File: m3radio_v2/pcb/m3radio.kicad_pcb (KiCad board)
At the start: 2 copper layers, 40 x 40 mm, 65 parts, among them IC1 NCP380, IC101 STM32F405RxTx, IC102 MCP2562, IC2 NC7SZ04, IC201 Si4460, IC3 CS2100-CP, IC4 SL18860DC, IC5 MAX_M8Q, IC6 SN74LVC1G0832, J101 WEST TOP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

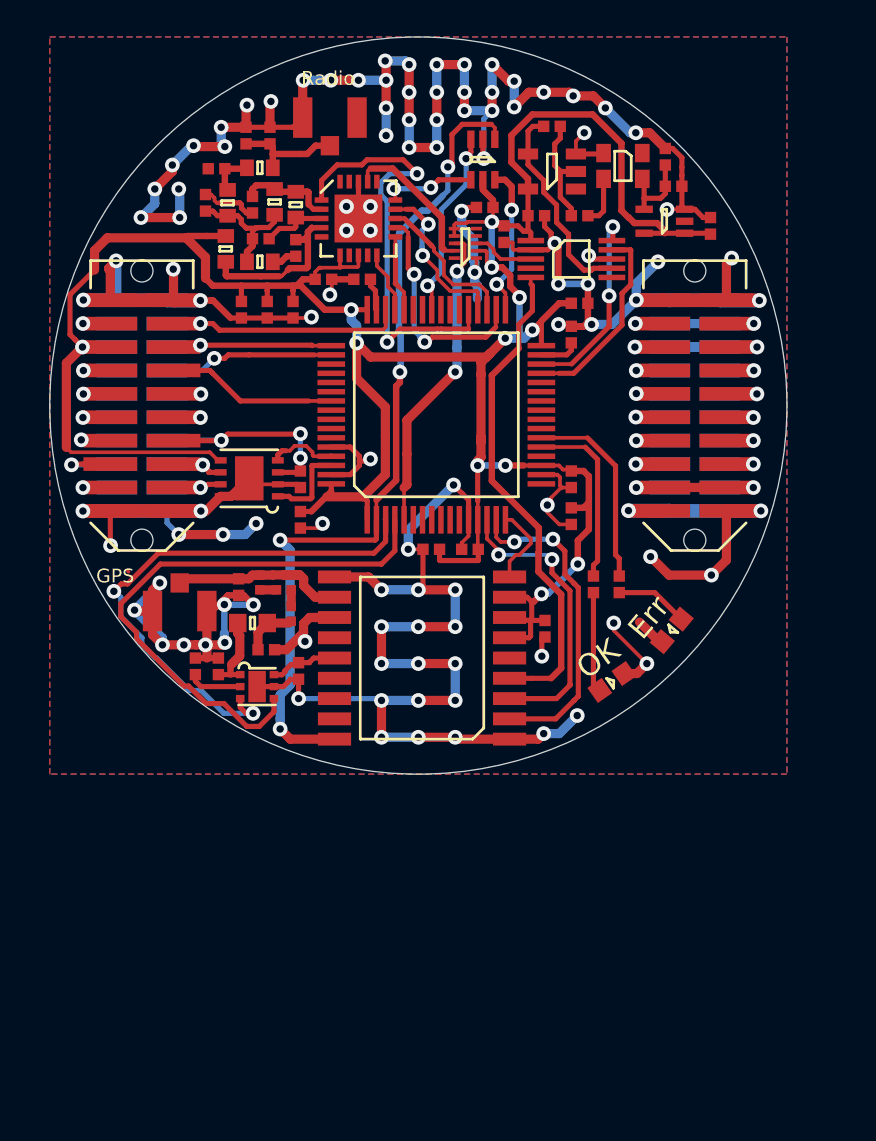
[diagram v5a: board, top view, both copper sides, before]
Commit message: Actually connect gps pps to tim2
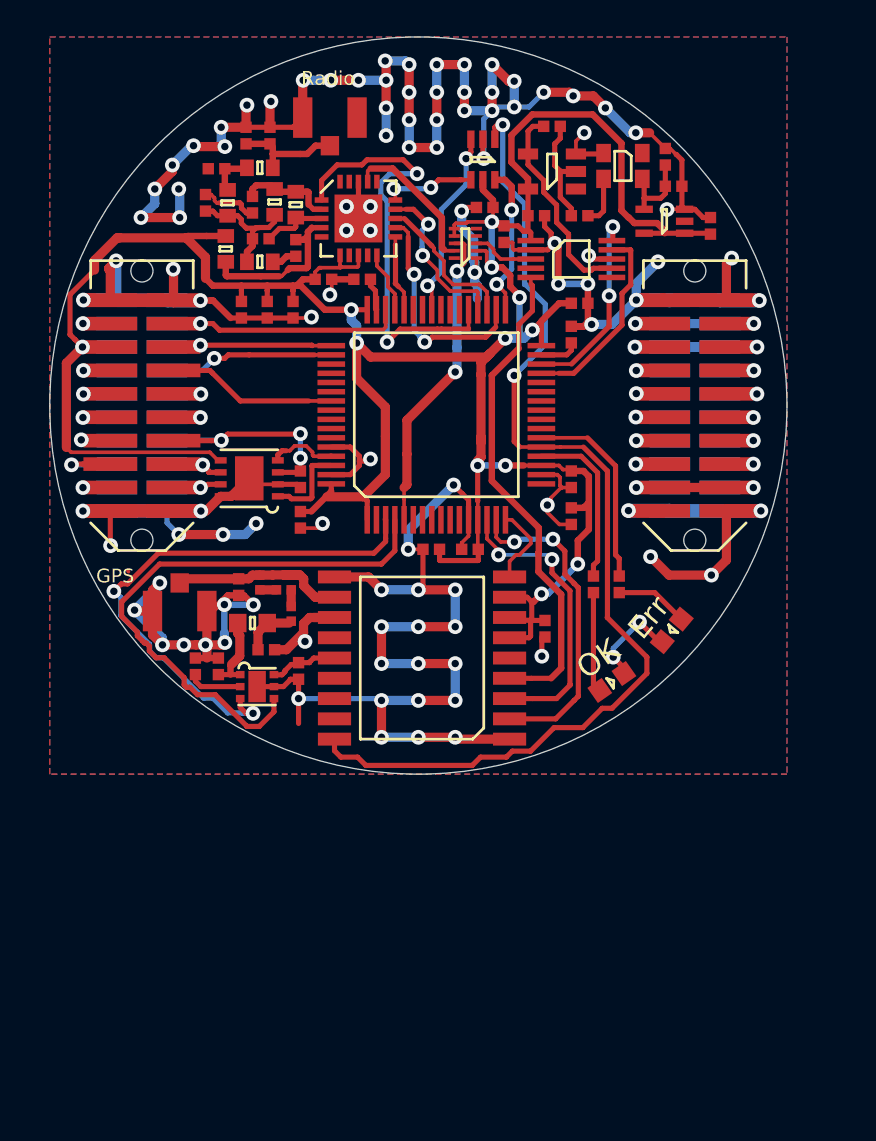
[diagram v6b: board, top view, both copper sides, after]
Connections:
- net /Radio/Radio_GPIO1 renamed /Radio_GPIO1
- net /Radio/Radio_SCLK renamed /Radio_SCLK
- net /Radio/Radio_SDI renamed /Radio_SDI
- net /Radio/Radio_SDN renamed /Radio_SDN
- net /Radio/Radio_SDO renamed /Radio_SDO
- net /Radio/Radio_XIN renamed /Radio_CLK
- net /Radio/Radio_nIRQ renamed /Radio_nIRQ
- IC101 pad 2: /GPS_PPS -> (no net)
- IC101 pad 20: (no net) -> /LED_GRN
- IC101 pad 21: /LED_GRN -> /GPS_PPS
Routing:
- net /GPS_PPS: track 46.3 -> 57.6 mm, vias 4 -> 2
- net GND: track 331.6 -> 328.4 mm, vias 107 -> 104
- net /LED_GRN: track 9.75 -> 9.12 mm

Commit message: Reduce radio board diameter
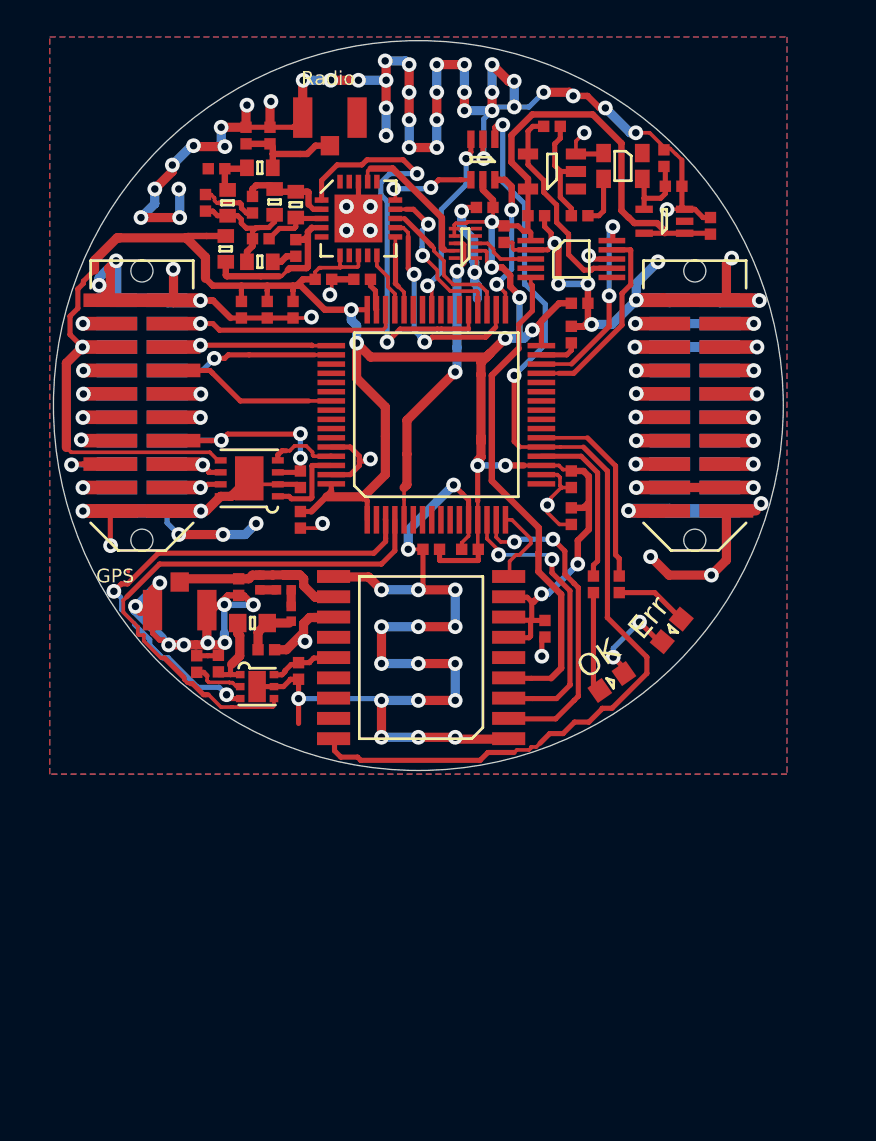
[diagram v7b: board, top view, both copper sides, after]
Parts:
- moved C3 0.15 mm to (89.2, 114.0)
- moved R2 0.15 mm to (88.0, 114.0)
- moved C8 0.11 mm to (113.3, 86.6)
- moved IC5 0.06 mm to (100.2, 113.7)
- moved P101 0.05 mm to (87.0, 111.1)
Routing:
- net GND: track 328.4 -> 331.2 mm
- net /ANT_~FLAG: track 29.5 -> 26.9 mm
- net /ANT_~EN: track 30.7 -> 29.4 mm
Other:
- board size 40 x 40 mm -> 39.6 x 39.6 mm

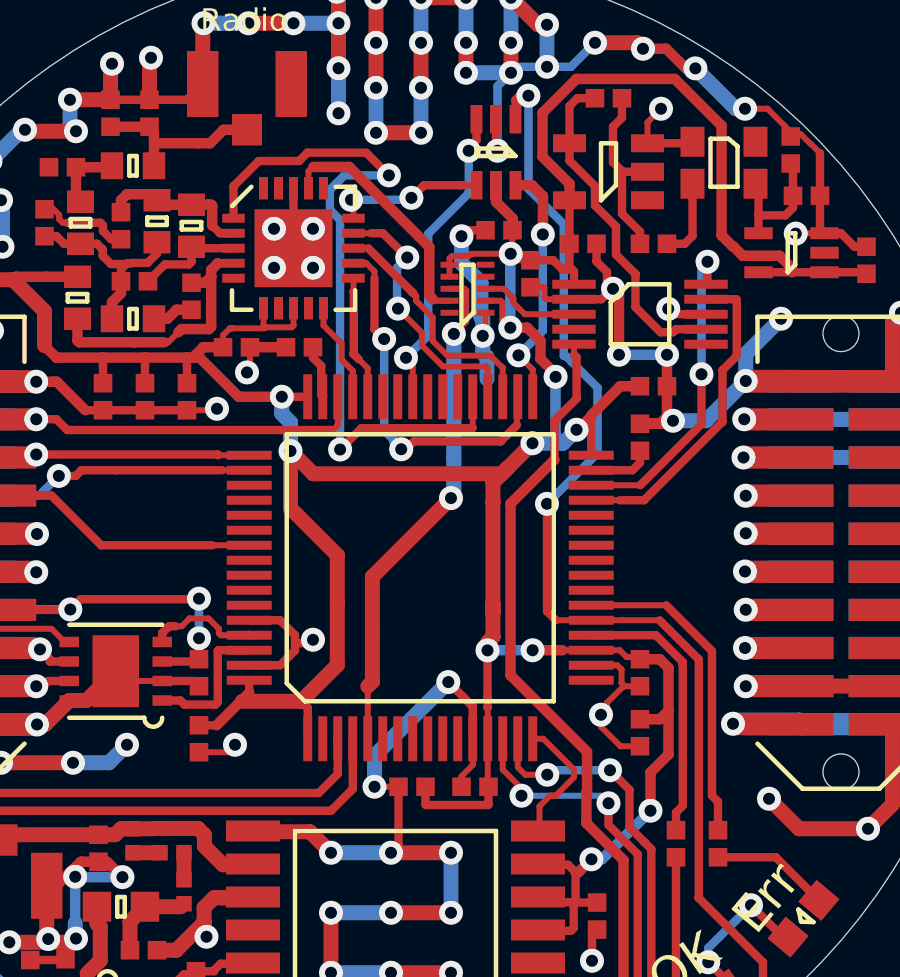
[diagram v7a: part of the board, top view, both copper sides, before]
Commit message: moved Radio nSel to PA3 e.g. TIM2
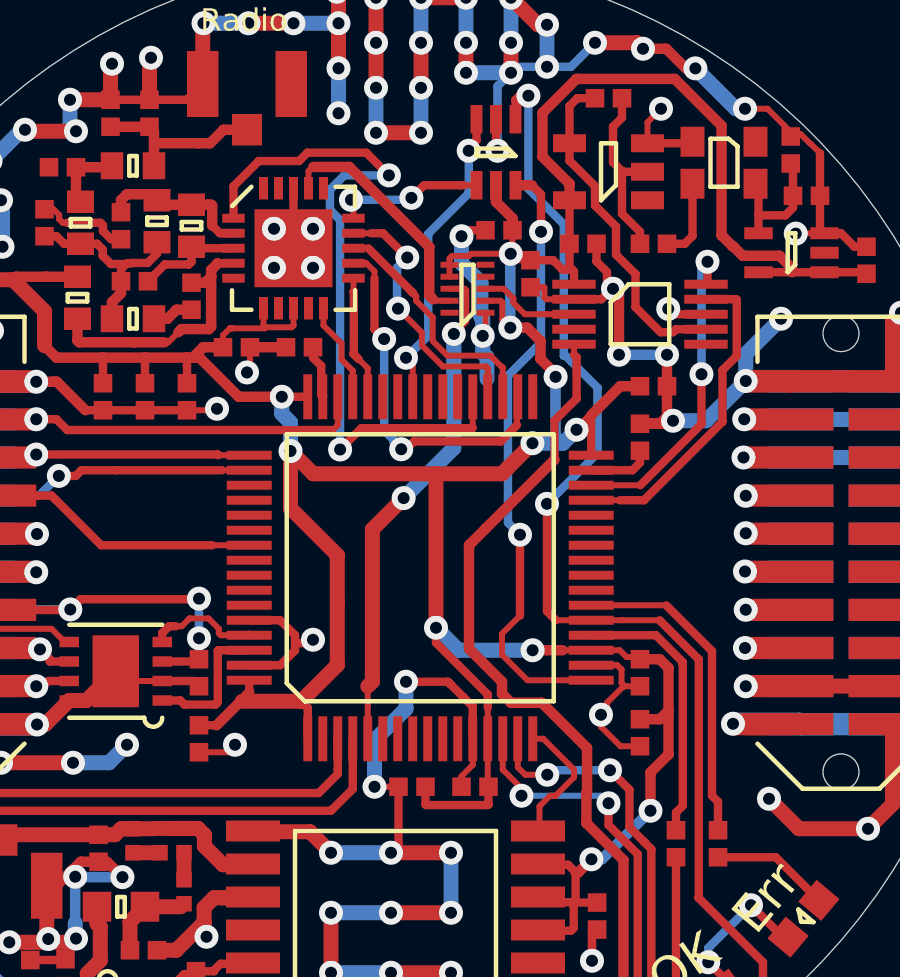
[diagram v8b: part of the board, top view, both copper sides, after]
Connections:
- IC101 pad 10: (no net) -> Net-(IC101-Pad10)
- IC101 pad 11: (no net) -> Net-(IC101-Pad11)
- IC101 pad 17: (no net) -> /Radio_nSEL
- IC101 pad 2: (no net) -> Net-(IC101-Pad2)
- IC101 pad 23: (no net) -> Net-(IC101-Pad23)
- IC101 pad 24: (no net) -> Net-(IC101-Pad24)
- IC101 pad 25: (no net) -> Net-(IC101-Pad25)
- IC101 pad 26: (no net) -> Net-(IC101-Pad26)
- IC101 pad 27: (no net) -> Net-(IC101-Pad27)
- IC101 pad 28: (no net) -> Net-(IC101-Pad28)
- IC101 pad 33: /Radio_nSEL -> Net-(IC101-Pad33)
- IC101 pad 38: (no net) -> Net-(IC101-Pad38)
- IC101 pad 39: (no net) -> Net-(IC101-Pad39)
- IC101 pad 40: (no net) -> Net-(IC101-Pad40)
- IC101 pad 42: (no net) -> Net-(IC101-Pad42)
- IC101 pad 43: (no net) -> Net-(IC101-Pad43)
- IC101 pad 51: (no net) -> Net-(IC101-Pad51)
- IC101 pad 52: (no net) -> Net-(IC101-Pad52)
- IC101 pad 53: (no net) -> Net-(IC101-Pad53)
- IC101 pad 54: (no net) -> Net-(IC101-Pad54)
- IC101 pad 56: (no net) -> Net-(IC101-Pad56)
- IC101 pad 57: (no net) -> Net-(IC101-Pad57)
- IC101 pad 58: (no net) -> Net-(IC101-Pad58)
- IC101 pad 59: (no net) -> Net-(IC101-Pad59)
- IC101 pad 6: (no net) -> Net-(IC101-Pad6)
- IC101 pad 7: (no net) -> Net-(IC101-Pad7)
- IC101 pad 8: (no net) -> Net-(IC101-Pad8)
- IC101 pad 9: (no net) -> Net-(IC101-Pad9)
- IC2 pad 1: (no net) -> Net-(IC2-Pad1)
- IC201 pad 16: (no net) -> Net-(IC201-Pad16)
- IC201 pad 19: (no net) -> Net-(IC201-Pad19)
- IC201 pad 20: (no net) -> Net-(IC201-Pad20)
- IC201 pad 5: (no net) -> Net-(IC201-Pad5)
- IC201 pad 7: (no net) -> Net-(IC201-Pad7)
- IC201 pad 9: (no net) -> Net-(IC201-Pad9)
- IC3 pad 4: (no net) -> Net-(IC3-Pad4)
- IC3 pad 6: (no net) -> Net-(IC3-Pad6)
- IC4 pad 10: (no net) -> Net-(IC4-Pad10)
- IC4 pad 4: (no net) -> Net-(IC4-Pad4)
- IC4 pad 5: (no net) -> Net-(IC4-Pad5)
- IC5 pad 13: (no net) -> Net-(IC5-Pad13)
- IC5 pad 15: (no net) -> Net-(IC5-Pad15)
- IC5 pad 16: (no net) -> Net-(IC5-Pad16)
- IC5 pad 17: (no net) -> Net-(IC5-Pad17)
- IC5 pad 5: (no net) -> Net-(IC5-Pad5)
- U1 pad 2: (no net) -> Net-(U1-Pad2)
- Y1 pad 1: (no net) -> Net-(Y1-Pad1)
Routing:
- net /Radio_nSEL: track 8.29 -> 20.5 mm
- net 3v3: track 161.7 -> 163.6 mm
- net /GPS_TIM1: track 26.8 -> 28.5 mm
- net GND: track 331.2 -> 332.1 mm
